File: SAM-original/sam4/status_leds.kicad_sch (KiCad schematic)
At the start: 7 parts

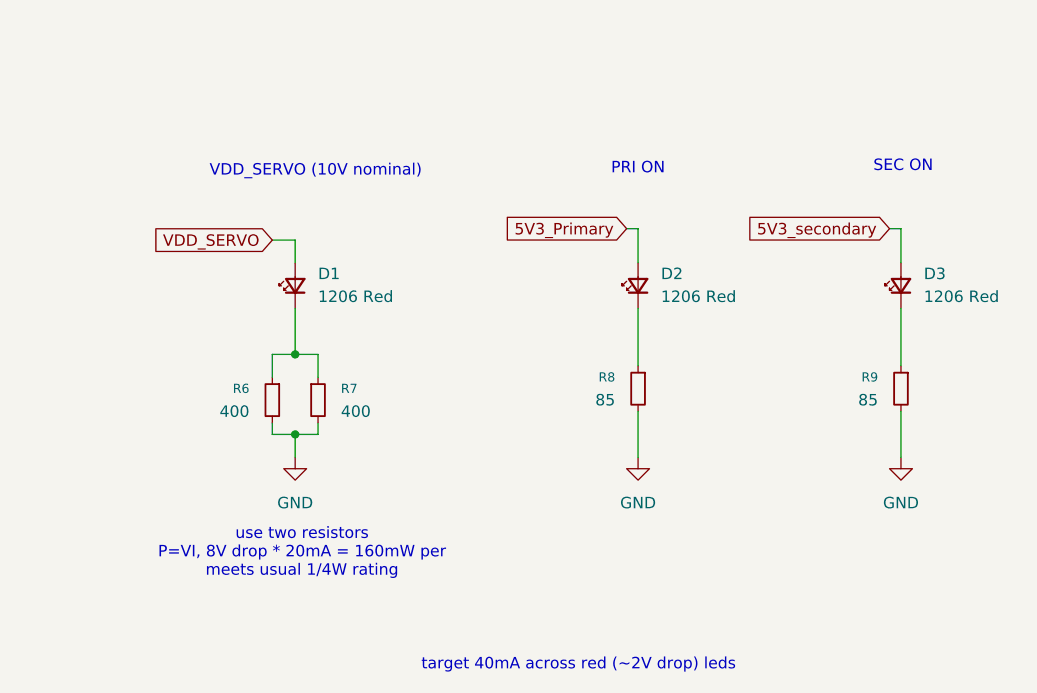
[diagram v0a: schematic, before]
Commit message: add updated SAM4 routing (DRC clean) + model
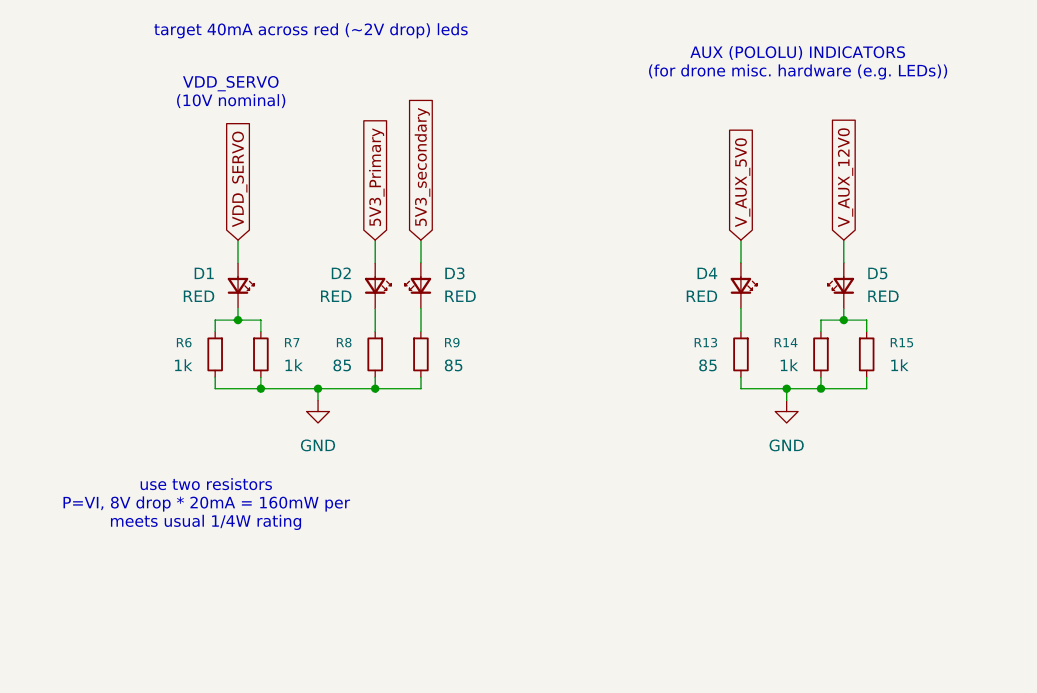
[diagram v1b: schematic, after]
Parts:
- added D4, D5: RED, LED_SMD:LED_0603_1608Metric_Pad1.05x0.95mm_HandSolder, symbol Device:LED_Small
- added R13: 85, Resistor_SMD:R_1206_3216Metric, symbol Device:R_Small
- added R14, R15: 1k, Resistor_SMD:R_1206_3216Metric, symbol Device:R_Small
- D1, D2, D3: value 1206 Red -> RED; footprint LED_SMD:LED_1206_3216Metric -> LED_SMD:LED_0603_1608Metric_Pad1.05x0.95mm_HandSolder; LCSC (none) -> C2286
- R6, R7: value 400 -> 1k; LCSC (none) -> C4410
- R8, R9: LCSC (none) -> C17901
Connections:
- net GND: now also R13.2, R14.2, R15.2
- new net: D4.1 (K), R13.1
- new net: D5.1 (K), R14.1, R15.1
- new net V_AUX_12V0: D5.2 (A)
- new net V_AUX_5V0: D4.2 (A)
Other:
- note added: "AUX (POLOLU) INDICATORS (for drone misc. hardware (e.g. LEDs))"
- note removed: "PRI ON"
- note removed: "SEC ON"
- moved on the sheet: D1, D2, D3, R6, R7, R8, R9
